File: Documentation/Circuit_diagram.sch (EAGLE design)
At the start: 13 parts

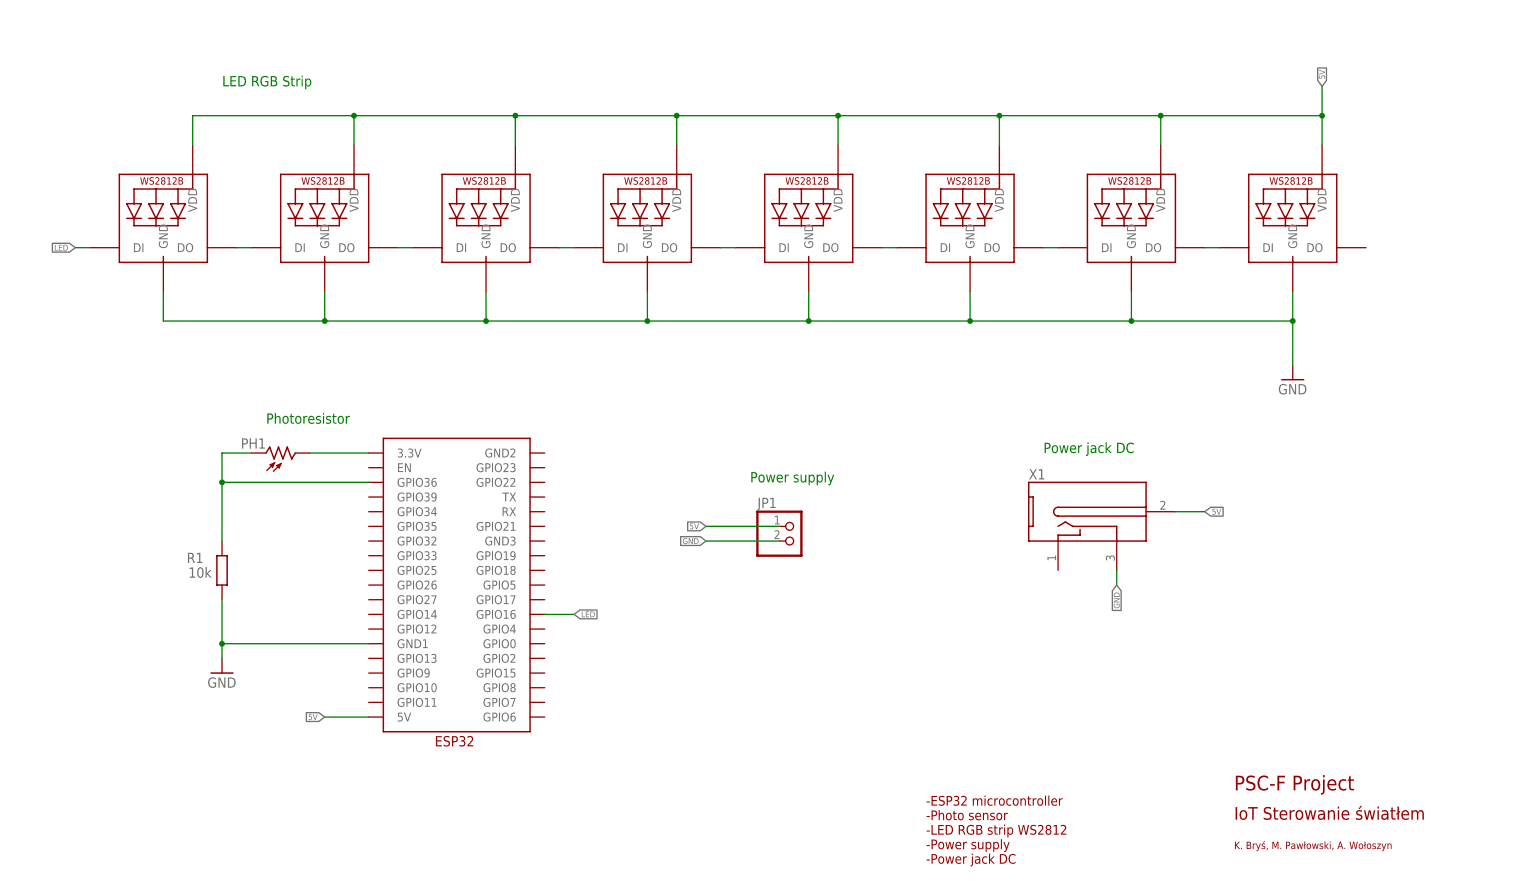
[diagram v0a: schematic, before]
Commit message: Merged PR 25: fix/circut-esp32-pinout
fix: add photos and fix circut schemat
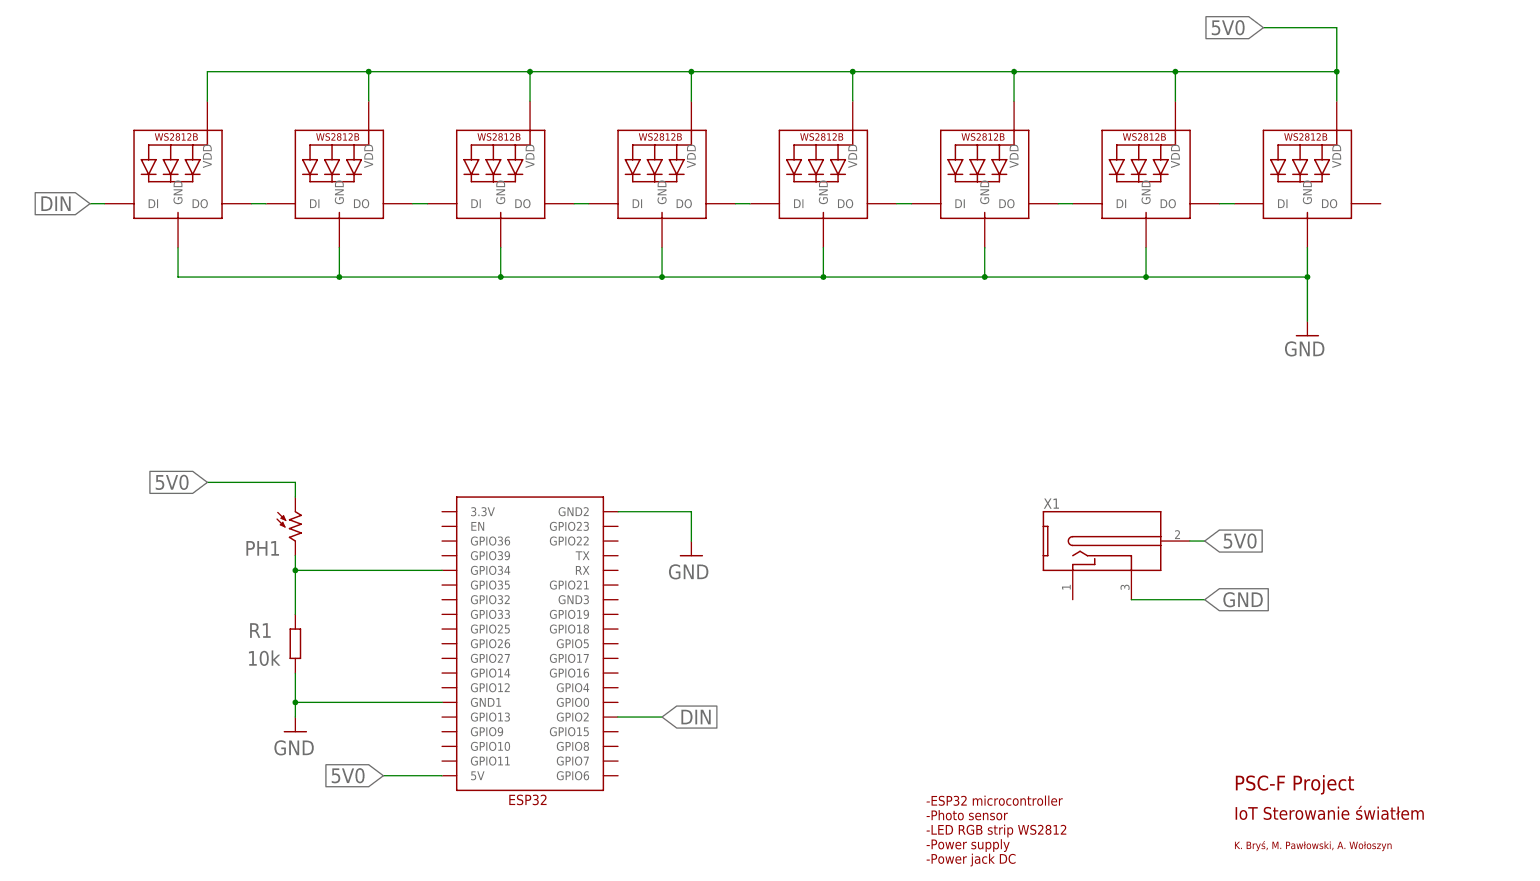
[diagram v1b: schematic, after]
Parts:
- removed JP1: (no value), pinhead:PINHD-1X2
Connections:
- removed net 5V: JP1.1, LED1.VDD, LED2.VDD, LED3.VDD, LED4.VDD, LED5.VDD, LED6.VDD, LED7.VDD, LED8.VDD, U$2.5V, X1.3
- removed net LED: LED1.DI, U$2.GPIO16
- removed net N$10: PH1.2, U$2.3.3V
- removed net N$11: PH1.1, R1.1, U$2.GPIO36
- new net 5V0: LED1.VDD, LED2.VDD, LED3.VDD, LED4.VDD, LED5.VDD, LED6.VDD, LED7.VDD, LED8.VDD, PH1.1, U$2.5V, X1.3
- new net DIN: LED1.DI, U$2.GPIO2
- new net N$9: PH1.2, R1.1, U$2.GPIO34
- net GND: now also U$2.GND2; no longer JP1.2
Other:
- note removed: "LED RGB Strip"
- note removed: "Photoresistor"
- note removed: "Power jack DC"
- note removed: "Power supply"
- moved on the sheet: PH1, R1, X1

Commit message: fix: instruction fix
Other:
- note added: "IoT Smart Light Project"
- note added: "Silesian University of Technology"
- note removed: "IoT Sterowanie światłem"
- note removed: "PSC-F Project"
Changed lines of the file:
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@@
 <sheet>
 <plain>
-<text x="292.1" y="-45.72" size="2.54" layer="94">PSC-F Project</text>
-<text x="292.1" y="-50.8" size="2.1844" layer="94">IoT Sterowanie światłem</text>
+<text x="292.1" y="-45.72" size="2.54" layer="94">IoT Smart Light Project</text>
+<text x="292.1" y="-50.8" size="1.778" layer="94">Silesian University of Technology</text>
 <text x="292.1" y="-55.88" size="1.27" layer="94">K. Bryś, M. Pawłowski, A. Wołoszyn</text>
 <text x="238.76" y="-58.42" size="1.6764" layer="94">-ESP32 microcontroller
